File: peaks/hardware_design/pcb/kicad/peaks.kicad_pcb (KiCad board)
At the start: 2 copper layers, 38.7 x 106.7 mm, 91 parts, among them IC1 LM1117-3.3, IC2 LM4040B25, IC3 DAC8552, IC4 OPA2171, IC5 OPA2171, IC6 LM4040B10, J1 PJ301_THONKICONN6, J2 PJ301_THONKICONN6, J3 PJ301_THONKICONN6, J4 PJ301_THONKICONN6, Q1 8MHz, Q2 MMBT3904, Q3 MMBT3904, SW4 LP4OA1PBCT, SW6 LP4OA1PBCT

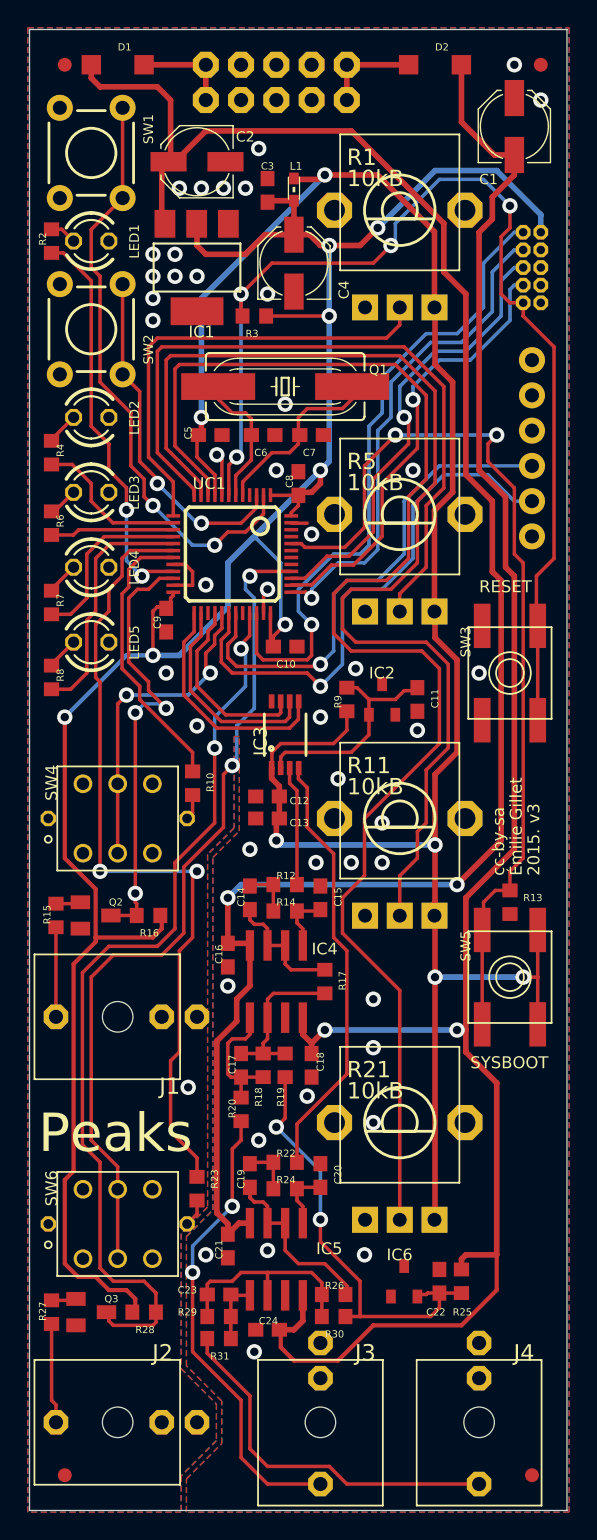
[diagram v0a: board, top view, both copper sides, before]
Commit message: peaks: smd boot + reset buttons
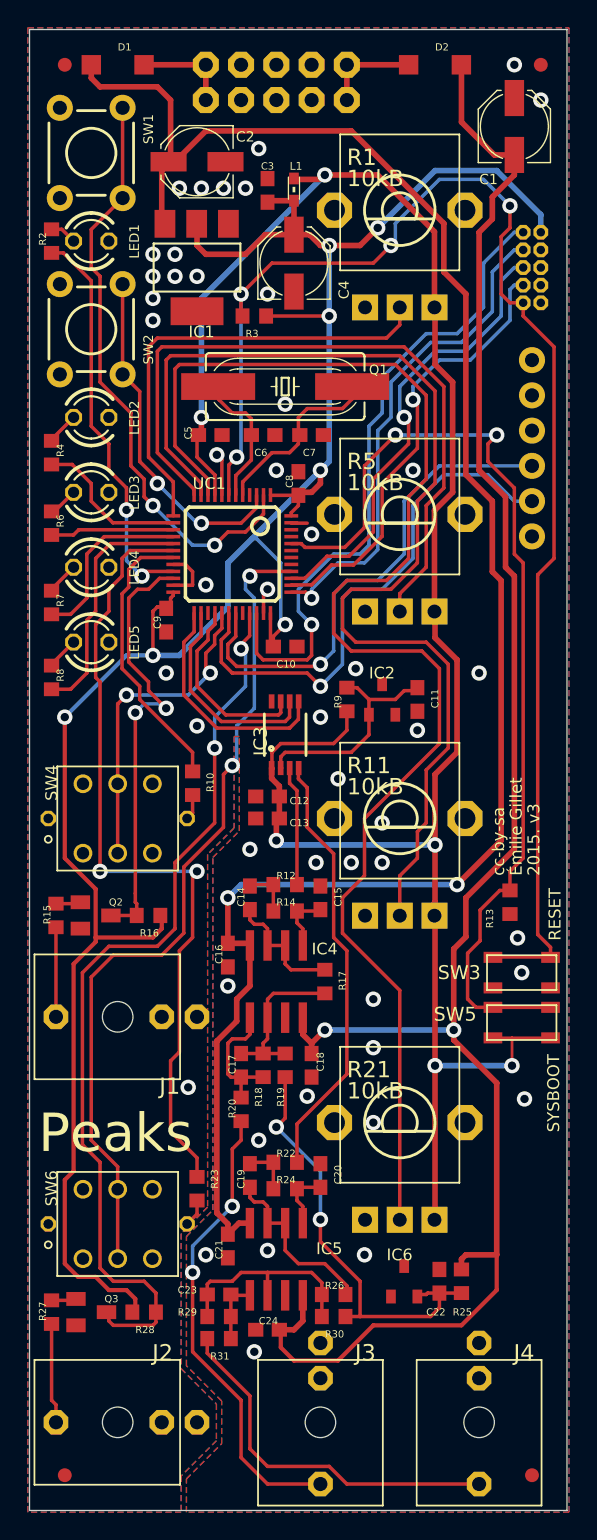
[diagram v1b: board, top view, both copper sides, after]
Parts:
- IC1: value LM1117-3.3 -> REG1117
- IC2: value LM4040B25 -> LM4041DBZ
- IC4, IC5: value OPA2171 -> TL072D
- IC6: value LM4040B10 -> LM4041DBZ
- JP1: value (none) -> M06SIP
- L1: value (none) -> WE-CBF_0603
- LED1, LED2, LED3, LED4, LED5: value (none) -> LED3MM
- SW1, SW2: value (none) -> TAC_SWITCHPTH
- SW3, SW5: value (none) -> EVQQ2; footprint peaks:EVQ-Q2 -> Library:k2-1808 pushbutton switch
- UC1: value STM32F103CBT6 -> STM32F103CB
- moved SW3 21.6 mm to (164.6, 119.6), turned to 0 degrees
- moved SW5 3.38 mm to (164.6, 123.2), turned to 180 degrees
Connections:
- net BI_OUT renamed Net-(IC4A-OUT)
- net BI_OUT1 renamed Net-(IC5A-OUT)
- net BOOT_FLASH renamed /peaks_1/BOOT_FLASH
- net DAC_MOSI renamed /peaks_1/DAC_MOSI
- net DAC_SCK renamed /peaks_1/DAC_SCK
- net DAC_SS renamed /peaks_1/DAC_SS
- net F_CV renamed Net-(IC4A--IN)
- net F_CV1 renamed Net-(IC5A--IN)
- net JTCK renamed /peaks_1/JTCK
- net JTDI renamed /peaks_1/JTDI
- net JTDO renamed /peaks_1/JTDO
- net JTMS renamed /peaks_1/JTMS
- net POT_1 renamed /peaks_1/POT_1
- net POT_2 renamed /peaks_1/POT_2
- net POT_3 renamed /peaks_1/POT_3
- net POT_4 renamed /peaks_1/POT_4
- net RESET renamed /peaks_1/RESET
- net RX renamed /peaks_1/RX
- net SW_DUAL renamed /peaks_1/SW_DUAL
- net SW_MODE renamed /peaks_1/SW_MODE
- net SW_TRIG_1 renamed /peaks_1/SW_TRIG_1
- net SW_TRIG_2 renamed /peaks_1/SW_TRIG_2
- net TRIG_1 renamed /peaks_1/TRIG_1
- net TRIG_2 renamed /peaks_1/TRIG_2
- net TX renamed /peaks_1/TX
- J3 pad P2: (no net) -> unconnected-(J3-2-PadP2)
- J4 pad P2: (no net) -> unconnected-(J4-2-PadP2)
- JP1 pad 2: (no net) -> unconnected-(JP1-Pad2)
- JP1 pad 3: (no net) -> unconnected-(JP1-Pad3)
- JP1 pad 6: (no net) -> unconnected-(JP1-Pad6)
- JP2 pad 7: (no net) -> unconnected-(JP2-Pad7)
- SW4 pad P1: (no net) -> unconnected-(SW4A-A1-PadP1)
- SW4 pad P4: (no net) -> unconnected-(SW4A-B1-PadP4)
- SW6 pad P1: (no net) -> unconnected-(SW6A-A1-PadP1)
- SW6 pad P4: (no net) -> unconnected-(SW6A-B1-PadP4)
- UC1 pad 27: (no net) -> unconnected-(UC1-PB14/SPI2_MISO/USART3_RTS/TIM1_CH2N-Pad27)
- UC1 pad 32: (no net) -> unconnected-(UC1-PA11/USART1_CTS/CAN_RX/TIM1_CH4/USBDM-Pad32)
- UC1 pad 4: (no net) -> unconnected-(UC1-PC15-OSC32_OUT-Pad4)
- UC1 pad 41: (no net) -> unconnected-(UC1-PB5/I2C1_SMBA-Pad41)
- UC1 pad 42: (no net) -> unconnected-(UC1-PB6/I2C1_SCL/TIM4_CH1-Pad42)
- UC1 pad 43: (no net) -> unconnected-(UC1-PB7/I2C1_SDA/TIM4_CH2-Pad43)
- UC1 pad 45: (no net) -> unconnected-(UC1-PB8/TIM4_CH3-Pad45)
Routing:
- net /peaks_1/RESET: track 81.6 -> 102.4 mm
- net /peaks_1/BOOT_FLASH: track 66.5 -> 71.1 mm
- net +3V3_A: track 152.9 -> 150.4 mm
- net GND: vias 45 -> 48
- net /peaks_1/TRIG_2: vias 3 -> 2
